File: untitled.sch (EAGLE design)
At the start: 12 parts

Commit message: added drawings for lpkf  router or self cnc dxf export.
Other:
- note added: "Pin-assignments from Grbl 0.5"
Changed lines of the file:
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@@
 <text x="73.66" y="43.18" size="1.778" layer="91">ENABLE</text>
 <text x="76.2" y="40.64" size="1.778" layer="91">MS1</text>
+<text x="15.24" y="114.3" size="5.08" layer="91">Pin-assignments from Grbl 0.5</text>
 </plain>
 <instances>

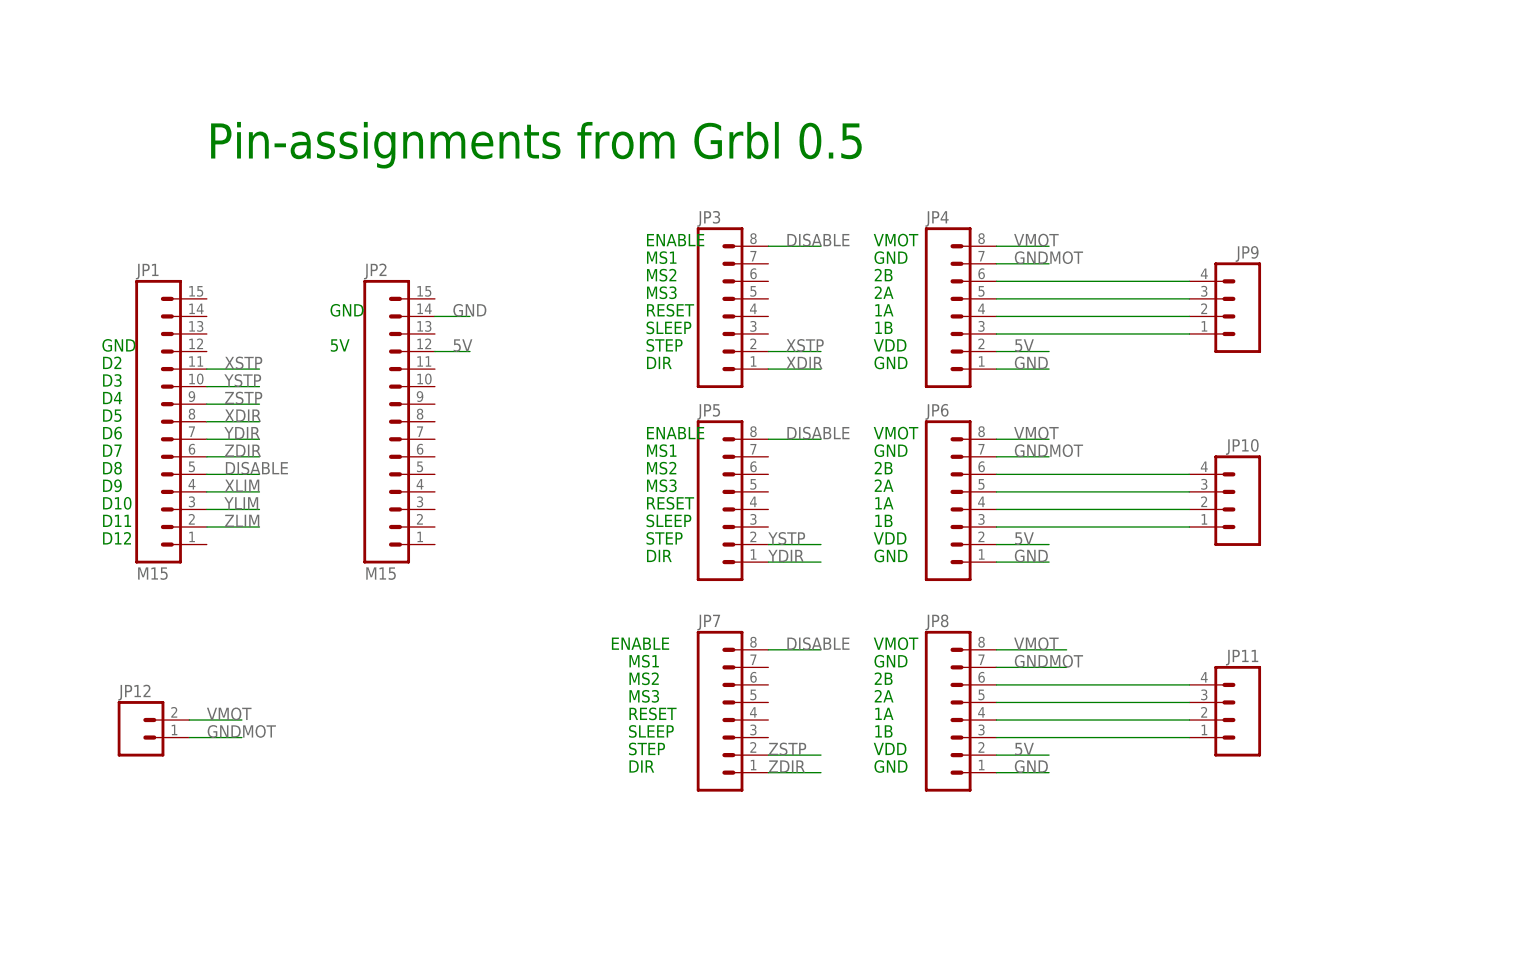
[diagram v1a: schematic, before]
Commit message: added ground planes
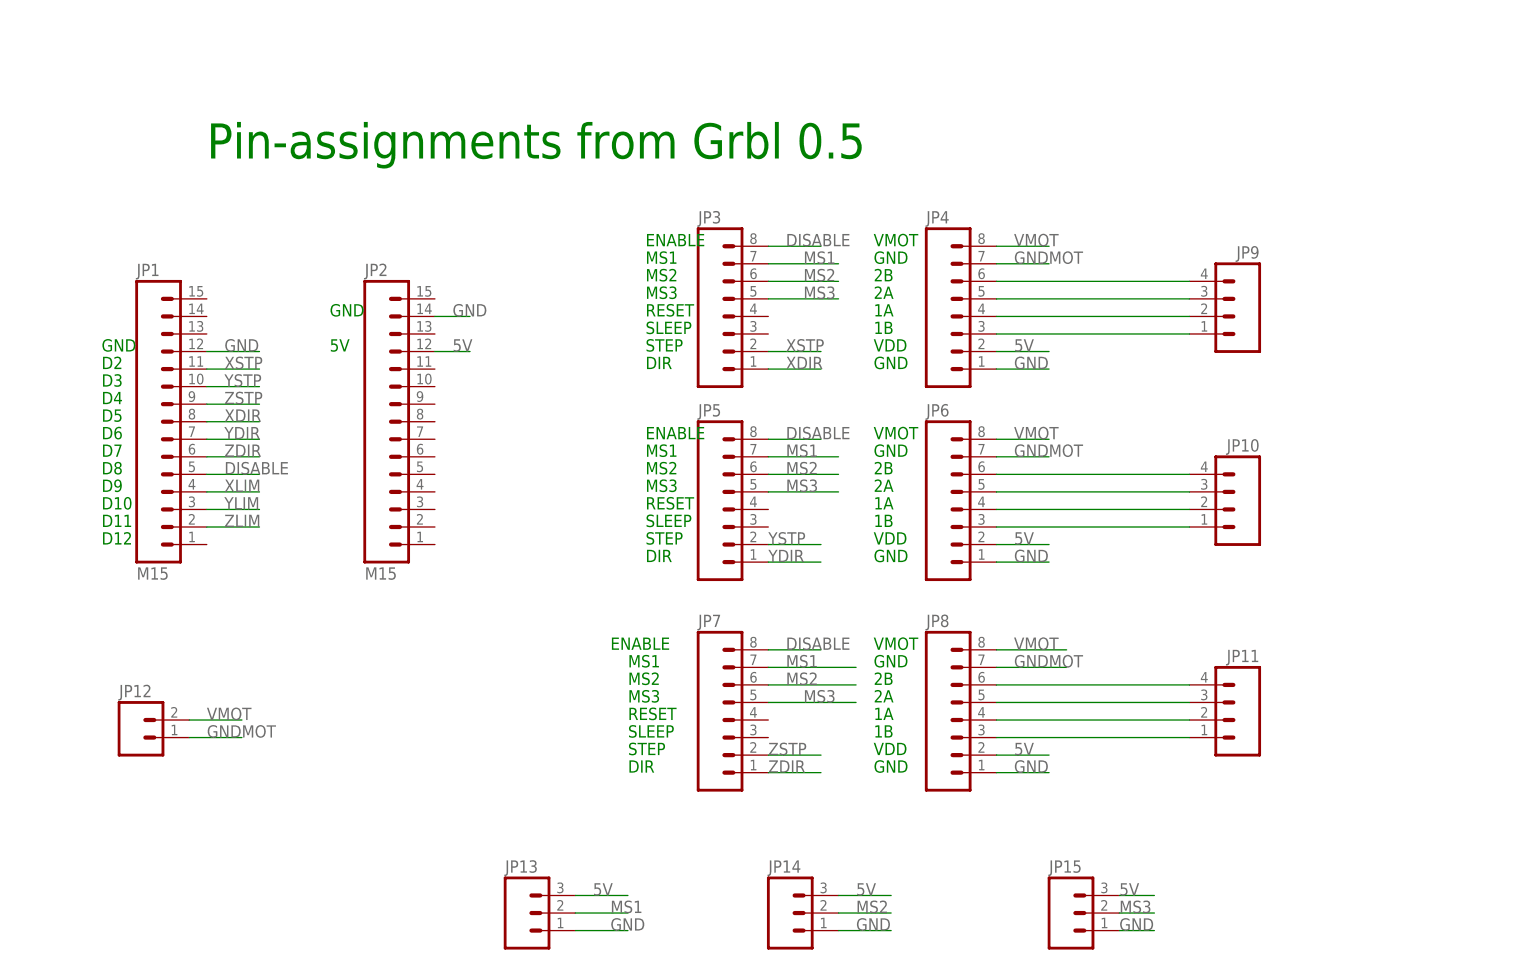
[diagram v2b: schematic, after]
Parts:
- added JP13, JP14, JP15: (no value), SparkFun:M03PTH
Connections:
- new net MS1: JP13.2, JP3.7, JP5.7, JP7.7
- new net MS2: JP14.2, JP3.6, JP5.6, JP7.6
- new net MS3: JP15.2, JP3.5, JP5.5, JP7.5
- net 5V: now also JP13.3, JP14.3, JP15.3
- net GND: now also JP1.12, JP13.1, JP14.1, JP15.1
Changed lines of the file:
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@@
 <part name="JP11" library="SparkFun" deviceset="M04" device="LONGPADS"/>
 <part name="JP12" library="SparkFun" deviceset="M02" device="LOCK_LONGPADS"/>
+<part name="JP13" library="SparkFun" deviceset="M03" device="PTH"/>
+<part name="JP14" library="SparkFun" deviceset="M03" device="PTH"/>
+<part name="JP15" library="SparkFun" deviceset="M03" device="PTH"/>
 </parts>
 <sheets>
@@
 <instance part="JP11" gate="G$1" x="162.56" y="33.02" rot="MR0"/>
 <instance part="JP12" gate="G$1" x="5.08" y="30.48"/>
+<instance part="JP13" gate="G$1" x="60.96" y="5.08"/>
+<instance part="JP14" gate="G$1" x="99.06" y="5.08"/>
+<instance part="JP15" gate="G$1" x="139.7" y="5.08"/>
 </instances>
 <busses>
@@
 <label x="132.08" y="58.42" size="1.778" layer="95"/>
 </segment>
+<segment>
+<pinref part="JP13" gate="G$1" pin="3"/>
+<wire x1="68.58" y1="7.62" x2="76.2" y2="7.62" width="0.1524" layer="91"/>
+<label x="71.12" y="7.62" size="1.778" layer="95"/>
+</segment>
+<segment>
+<pinref part="JP14" gate="G$1" pin="3"/>
+<wire x1="106.68" y1="7.62" x2="114.3" y2="7.62" width="0.1524" layer="91"/>
+<label x="109.22" y="7.62" size="1.778" layer="95"/>
+</segment>
+<segment>
+<pinref part="JP15" gate="G$1" pin="3"/>
+<wire x1="147.32" y1="7.62" x2="152.4" y2="7.62" width="0.1524" layer="91"/>
+<label x="147.32" y="7.62" size="1.778" layer="95"/>
+</segment>
 </net>
 <net name="GND" class="0">
@@
 <label x="132.08" y="83.82" size="1.778" layer="95"/>
 </segment>
+<segment>
+<pinref part="JP13" gate="G$1" pin="1"/>
+<wire x1="68.58" y1="2.54" x2="76.2" y2="2.54" width="0.1524" layer="91"/>
+<label x="73.66" y="2.54" size="1.778" layer="95"/>
+</segment>
+<segment>
+<pinref part="JP14" gate="G$1" pin="1"/>
+<wire x1="106.68" y1="2.54" x2="114.3" y2="2.54" width="0.1524" layer="91"/>
+<label x="109.22" y="2.54" size="1.778" layer="95"/>
+</segment>
+<segment>
+<pinref part="JP15" gate="G$1" pin="1"/>
+<wire x1="147.32" y1="2.54" x2="152.4" y2="2.54" width="0.1524" layer="91"/>
+<label x="147.32" y="2.54" size="1.778" layer="95"/>
+</segment>
+<segment>
+<pinref part="JP1" gate="G$1" pin="12"/>
+<wire x1="15.24" y1="86.36" x2="22.86" y2="86.36" width="0.1524" layer="91"/>
+<label x="17.78" y="86.36" size="1.778" layer="95"/>
+</segment>
 </net>
 <net name="YDIR" class="0">
@@
 </segment>
 </net>
+<net name="MS1" class="0">
+<segment>
+<pinref part="JP13" gate="G$1" pin="2"/>
+<wire x1="68.58" y1="5.08" x2="76.2" y2="5.08" width="0.1524" layer="91"/>
+<label x="73.66" y="5.08" size="1.778" layer="95"/>
+</segment>
+<segment>
+<pinref part="JP3" gate="G$1" pin="7"/>
+<wire x1="96.52" y1="99.06" x2="106.68" y2="99.06" width="0.1524" layer="91"/>
+<label x="101.6" y="99.06" size="1.778" layer="95"/>
+</segment>
+<segment>
+<pinref part="JP5" gate="G$1" pin="7"/>
+<wire x1="96.52" y1="71.12" x2="106.68" y2="71.12" width="0.1524" layer="91"/>
+<label x="99.06" y="71.12" size="1.778" layer="95"/>
+</segment>
+<segment>
+<pinref part="JP7" gate="G$1" pin="7"/>
+<wire x1="96.52" y1="40.64" x2="109.22" y2="40.64" width="0.1524" layer="91"/>
+<label x="99.06" y="40.64" size="1.778" layer="95"/>
+</segment>
+</net>
+<net name="MS2" class="0">
+<segment>
+<pinref part="JP14" gate="G$1" pin="2"/>
+<wire x1="106.68" y1="5.08" x2="114.3" y2="5.08" width="0.1524" layer="91"/>
+<label x="109.22" y="5.08" size="1.778" layer="95"/>
+</segment>
+<segment>
+<pinref part="JP3" gate="G$1" pin="6"/>
+<wire x1="96.52" y1="96.52" x2="106.68" y2="96.52" width="0.1524" layer="91"/>
+<label x="101.6" y="96.52" size="1.778" layer="95"/>
+</segment>
+<segment>
+<pinref part="JP5" gate="G$1" pin="6"/>
+<wire x1="96.52" y1="68.58" x2="106.68" y2="68.58" width="0.1524" layer="91"/>
+<label x="99.06" y="68.58" size="1.778" layer="95"/>
+</segment>
+<segment>
+<pinref part="JP7" gate="G$1" pin="6"/>
+<wire x1="96.52" y1="38.1" x2="109.22" y2="38.1" width="0.1524" layer="91"/>
+<label x="99.06" y="38.1" size="1.778" layer="95"/>
+</segment>
+</net>
+<net name="MS3" class="0">
+<segment>
+<pinref part="JP5" gate="G$1" pin="5"/>
+<wire x1="96.52" y1="66.04" x2="106.68" y2="66.04" width="0.1524" layer="91"/>
+<label x="99.06" y="66.04" size="1.778" layer="95"/>
+</segment>
+<segment>
+<pinref part="JP7" gate="G$1" pin="5"/>
+<wire x1="96.52" y1="35.56" x2="109.22" y2="35.56" width="0.1524" layer="91"/>
+<label x="101.6" y="35.56" size="1.778" layer="95"/>
+</segment>
+<segment>
+<pinref part="JP3" gate="G$1" pin="5"/>
+<wire x1="96.52" y1="93.98" x2="106.68" y2="93.98" width="0.1524" layer="91"/>
+<label x="101.6" y="93.98" size="1.778" layer="95"/>
+</segment>
+<segment>
+<pinref part="JP15" gate="G$1" pin="2"/>
+<wire x1="147.32" y1="5.08" x2="152.4" y2="5.08" width="0.1524" layer="91"/>
+<label x="147.32" y="5.08" size="1.778" layer="95"/>
+</segment>
+</net>

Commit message: connected sleep and rst, one was floating
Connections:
- new net N$1: JP5.3, JP5.4
- new net N$14: JP7.3, JP7.4
- new net N$15: JP3.3, JP3.4
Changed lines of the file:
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@@
+</segment>
+</net>
+<net name="N$1" class="0">
+<segment>
+<pinref part="JP5" gate="G$1" pin="4"/>
+<wire x1="96.52" y1="63.5" x2="101.6" y2="63.5" width="0.1524" layer="91"/>
+<wire x1="101.6" y1="63.5" x2="101.6" y2="60.96" width="0.1524" layer="91"/>
+<pinref part="JP5" gate="G$1" pin="3"/>
+<wire x1="101.6" y1="60.96" x2="96.52" y2="60.96" width="0.1524" layer="91"/>
+</segment>
+</net>
+<net name="N$14" class="0">
+<segment>
+<pinref part="JP7" gate="G$1" pin="4"/>
+<wire x1="96.52" y1="33.02" x2="101.6" y2="33.02" width="0.1524" layer="91"/>
+<wire x1="101.6" y1="33.02" x2="101.6" y2="30.48" width="0.1524" layer="91"/>
+<pinref part="JP7" gate="G$1" pin="3"/>
+<wire x1="101.6" y1="30.48" x2="96.52" y2="30.48" width="0.1524" layer="91"/>
+</segment>
+</net>
+<net name="N$15" class="0">
+<segment>
+<pinref part="JP3" gate="G$1" pin="3"/>
+<wire x1="96.52" y1="88.9" x2="101.6" y2="88.9" width="0.1524" layer="91"/>
+<wire x1="101.6" y1="88.9" x2="101.6" y2="91.44" width="0.1524" layer="91"/>
+<pinref part="JP3" gate="G$1" pin="4"/>
+<wire x1="101.6" y1="91.44" x2="96.52" y2="91.44" width="0.1524" layer="91"/>
 </segment>
 </net>

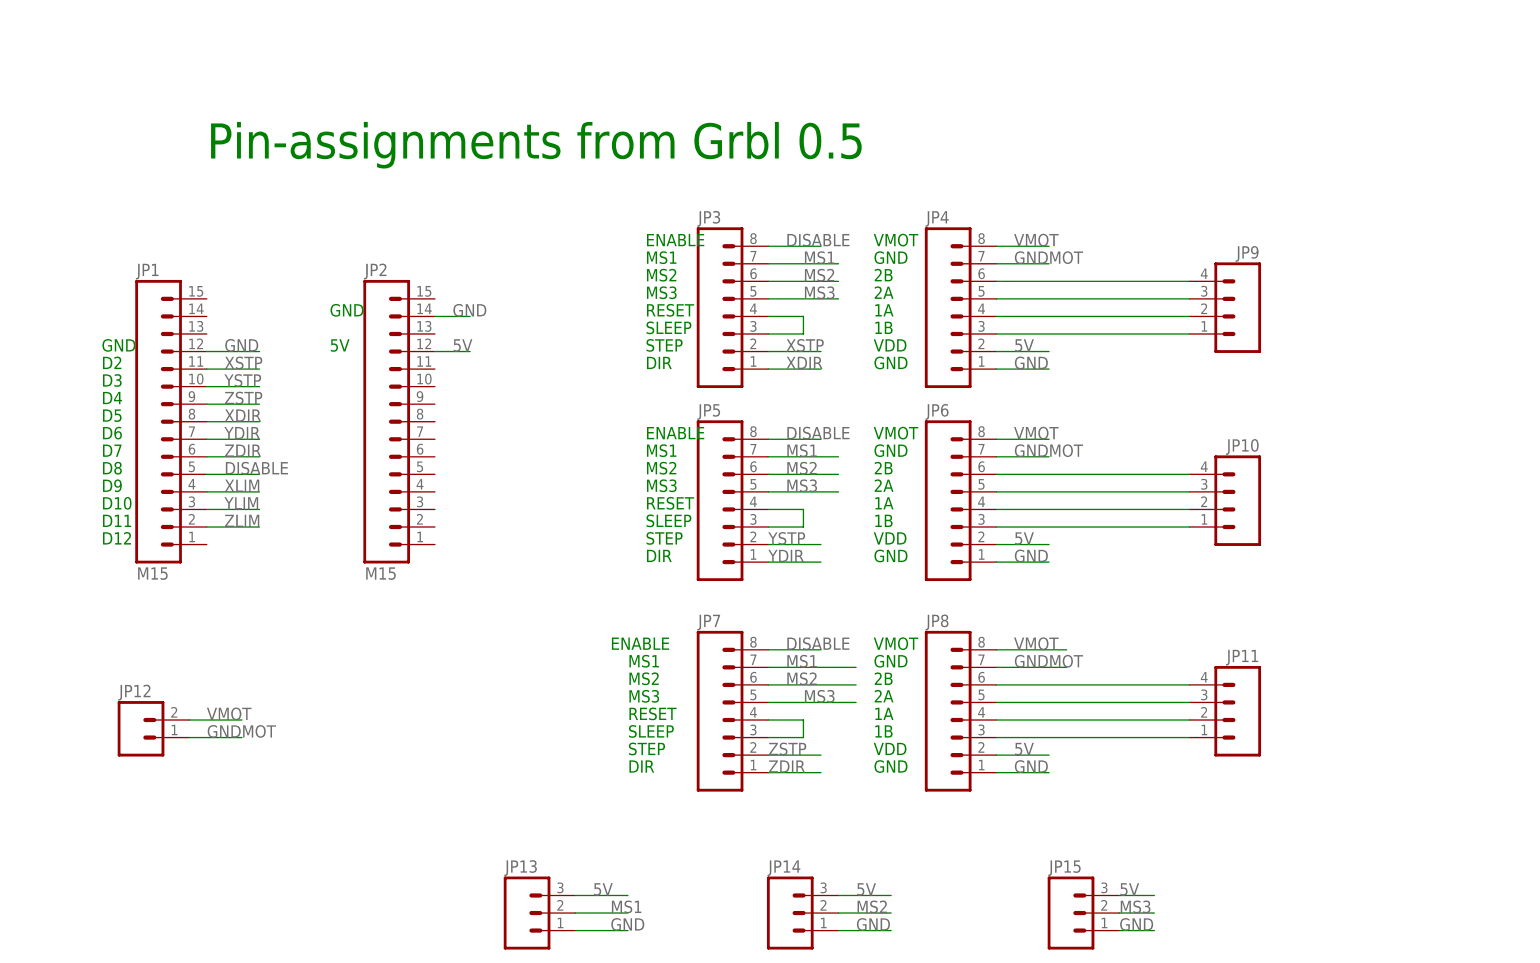
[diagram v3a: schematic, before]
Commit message: added gnd plane and rerouted
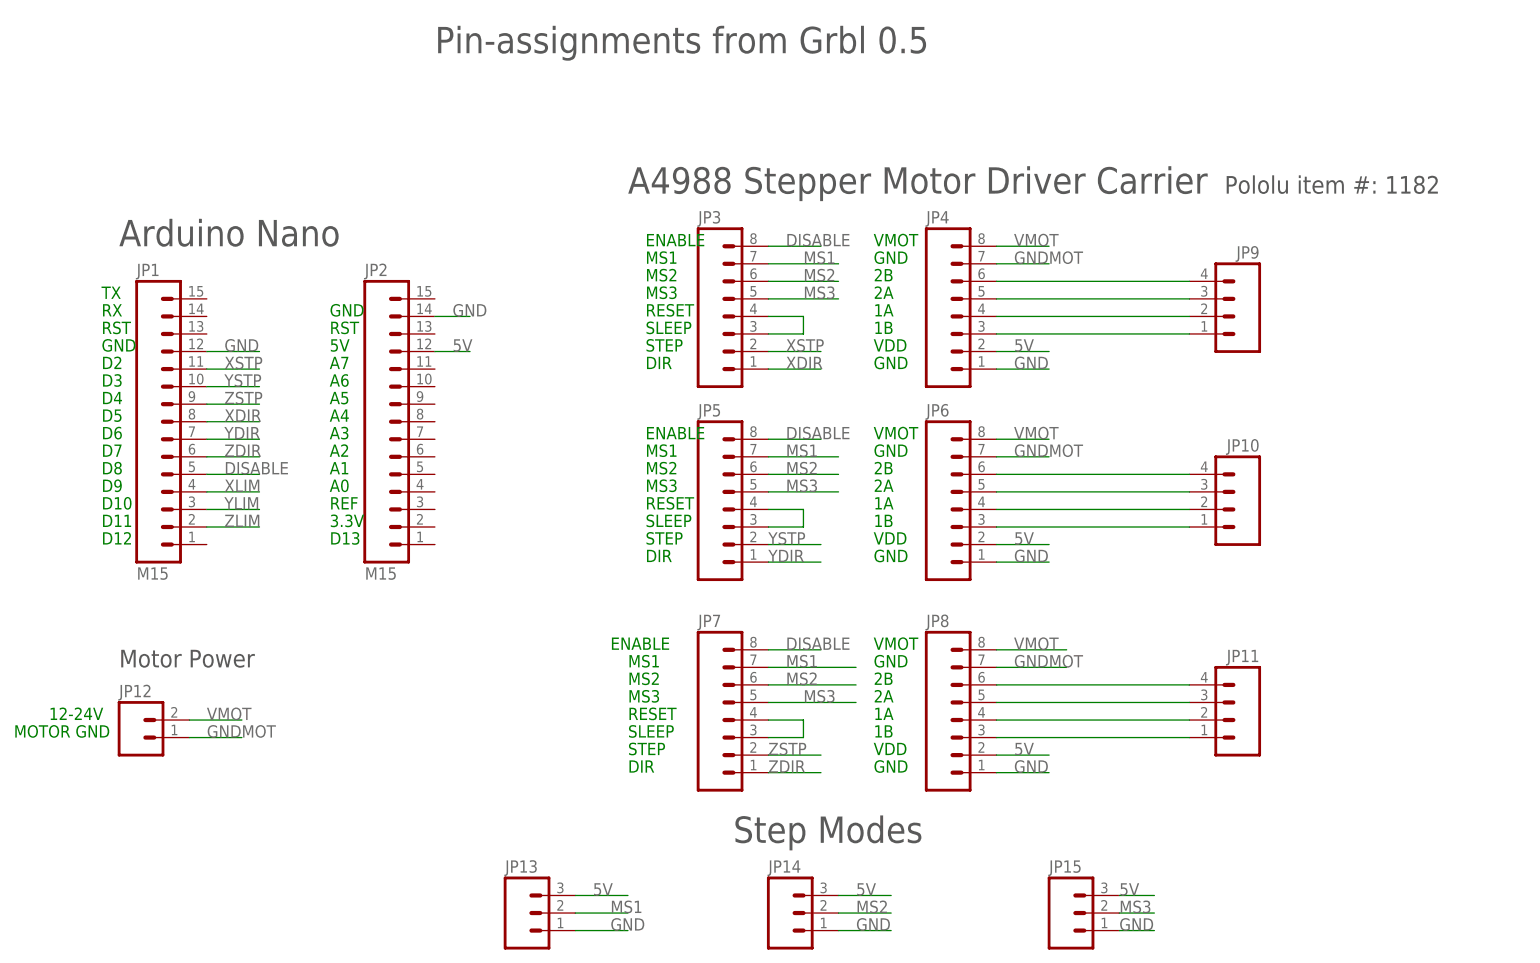
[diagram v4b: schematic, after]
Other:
- note added: "12-24V"
- note added: "3.3V"
- note added: "A0"
- note added: "A1"
- note added: "A2"
- note added: "A3"
- note added: "A4"
- note added: "A4988 Stepper Motor Driver Carrier"
- note added: "A5"
- note added: "A6"
- note added: "A7"
- note added: "Arduino Nano"
- note added: "D13"
- note added: "MOTOR GND"
- note added: "Motor Power"
- note added: "Pololu item #: 1182"
- note added: "REF"
- note added: "RST"
- note added: "RX"
- note added: "Step Modes"
- note added: "TX"
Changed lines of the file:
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@@
 <text x="73.66" y="43.18" size="1.778" layer="91">ENABLE</text>
 <text x="76.2" y="40.64" size="1.778" layer="91">MS1</text>
-<text x="15.24" y="114.3" size="5.08" layer="91">Pin-assignments from Grbl 0.5</text>
+<text x="48.26" y="129.54" size="3.81" layer="97">Pin-assignments from Grbl 0.5</text>
+<text x="91.44" y="15.24" size="3.81" layer="97">Step Modes</text>
+<text x="2.54" y="101.6" size="3.81" layer="97">Arduino Nano</text>
+<text x="76.2" y="109.22" size="3.81" layer="97">A4988 Stepper Motor Driver Carrier</text>
+<text x="162.56" y="109.22" size="2.54" layer="97">Pololu item #: 1182 </text>
+<text x="2.54" y="40.64" size="2.54" layer="97">Motor Power</text>
+<text x="33.02" y="88.9" size="1.778" layer="91">RST</text>
+<text x="0" y="88.9" size="1.778" layer="91">RST</text>
+<text x="0" y="91.44" size="1.778" layer="91">RX</text>
+<text x="0" y="93.98" size="1.778" layer="91">TX</text>
+<text x="33.02" y="83.82" size="1.778" layer="91">A7</text>
+<text x="33.02" y="81.28" size="1.778" layer="91">A6</text>
+<text x="33.02" y="78.74" size="1.778" layer="91">A5</text>
+<text x="33.02" y="76.2" size="1.778" layer="91">A4</text>
+<text x="33.02" y="73.66" size="1.778" layer="91">A3</text>
+<text x="33.02" y="71.12" size="1.778" layer="91">A2</text>
+<text x="33.02" y="68.58" size="1.778" layer="91">A1</text>
+<text x="33.02" y="66.04" size="1.778" layer="91">A0</text>
+<text x="33.02" y="63.5" size="1.778" layer="91">REF</text>
+<text x="33.02" y="60.96" size="1.778" layer="91">3.3V</text>
+<text x="33.02" y="58.42" size="1.778" layer="91">D13</text>
+<text x="-7.62" y="33.02" size="1.778" layer="91">12-24V</text>
+<text x="-12.7" y="30.48" size="1.778" layer="91">MOTOR GND</text>
 </plain>
 <instances>
